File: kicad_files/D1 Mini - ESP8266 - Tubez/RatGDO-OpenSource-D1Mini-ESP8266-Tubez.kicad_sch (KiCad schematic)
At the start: 30 parts, among them J1 Screw_Terminal_01x03, J2 Conn_01x11, J3 Screw_Terminal_01x02, Q1 2N7002, Q2 AO3400A, Q3 AO3400A, Q4 AO3400A, U1 WeMos_D1_mini, U2 K7805-500R3

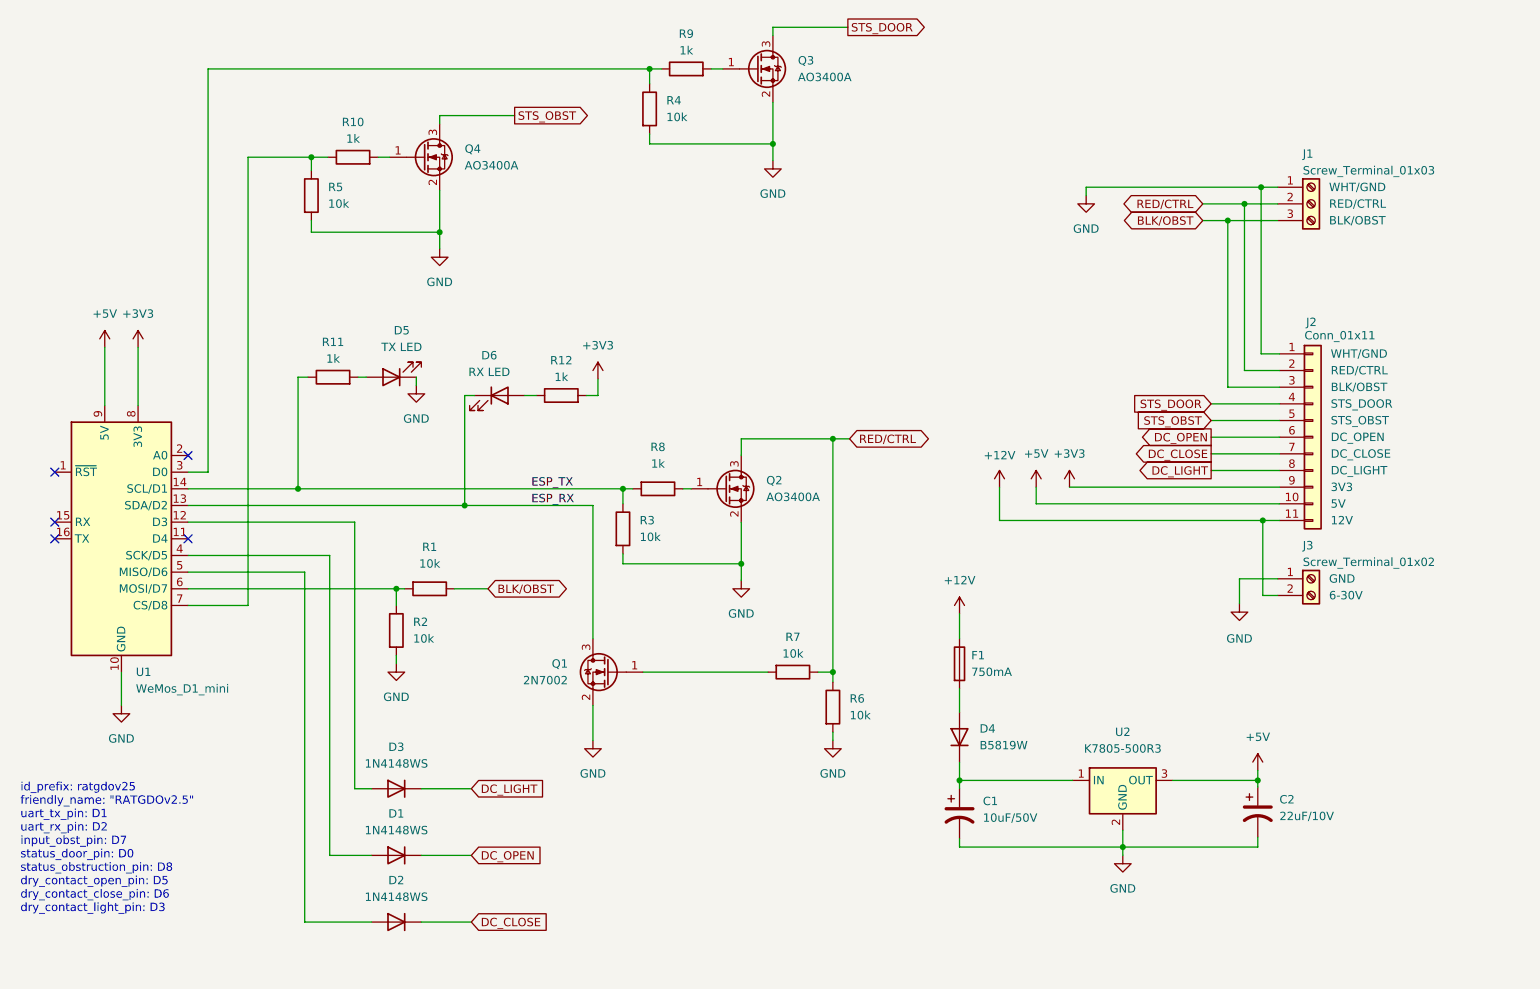
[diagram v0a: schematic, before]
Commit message: Added smt pcb jumper to switch between 5V or 3v3 supply
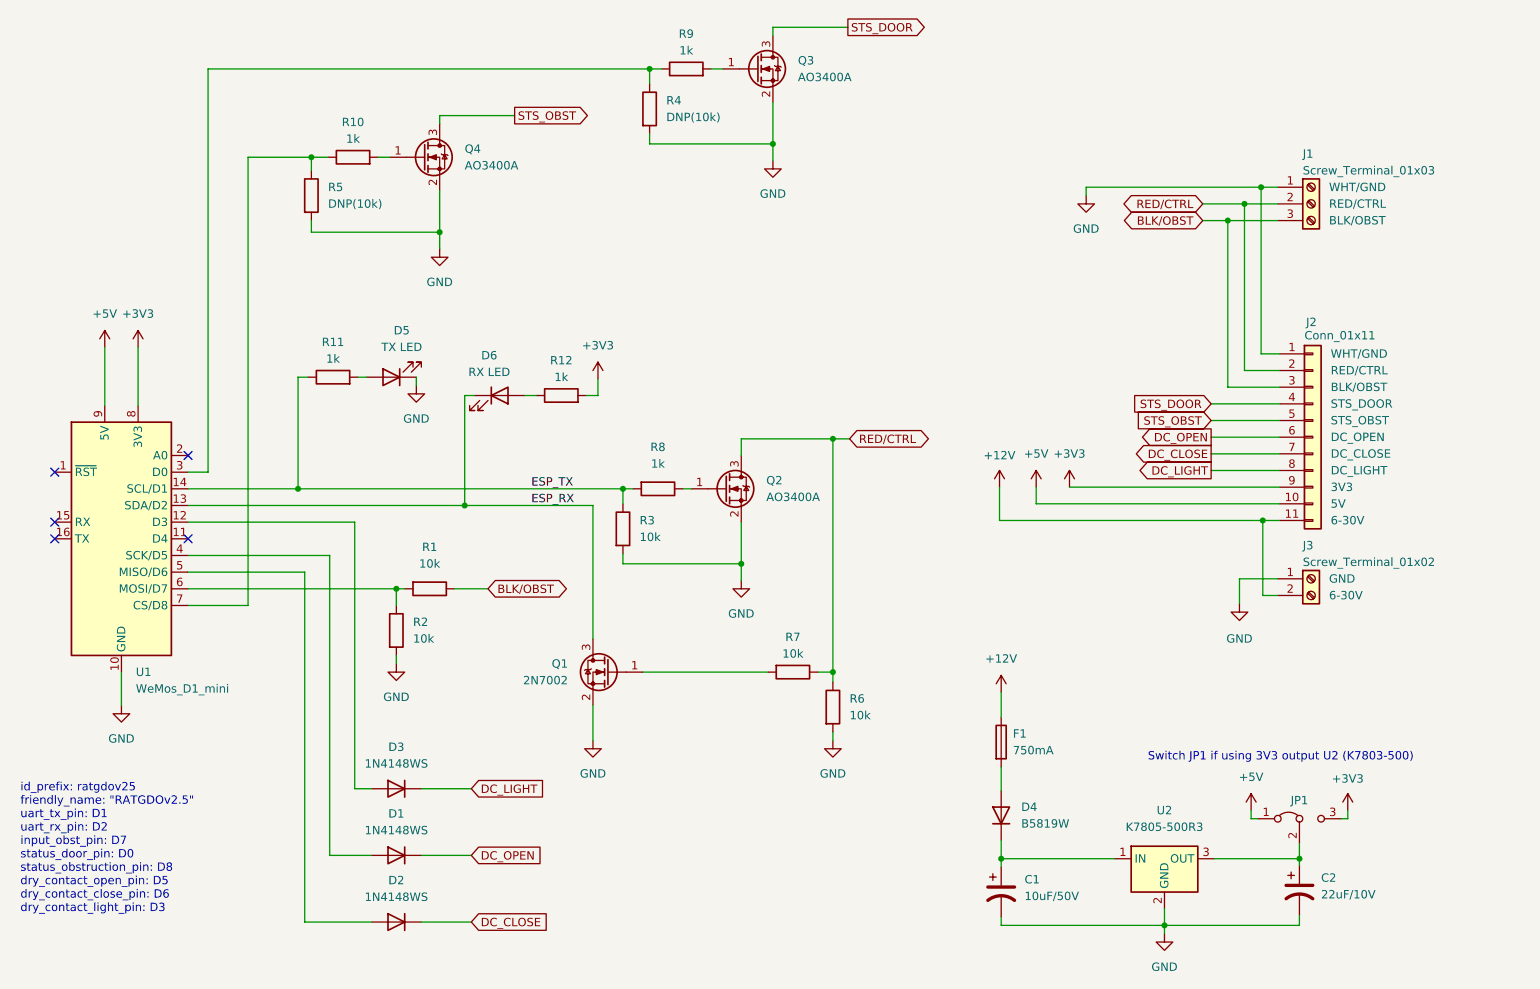
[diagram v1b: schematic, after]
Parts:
- added JP1: ~, Jumper:SolderJumper-3_P1.3mm_Bridged12_RoundedPad1.0x1.5mm, symbol Jumper:Jumper_3_Bridged12
- R4, R5: value 10k -> DNP(10k)
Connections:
- net +3V3: now also JP1.3 (B)
- net +5V: now also JP1.1 (A); no longer C2.1, U2.3 (OUT)
- new net: C2.1, JP1.2 (C), U2.3 (OUT)
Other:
- note added: "Switch JP1 if using 3V3 output U2 (K7803-500)"
- moved on the sheet: C1, C2, D4, F1, U2

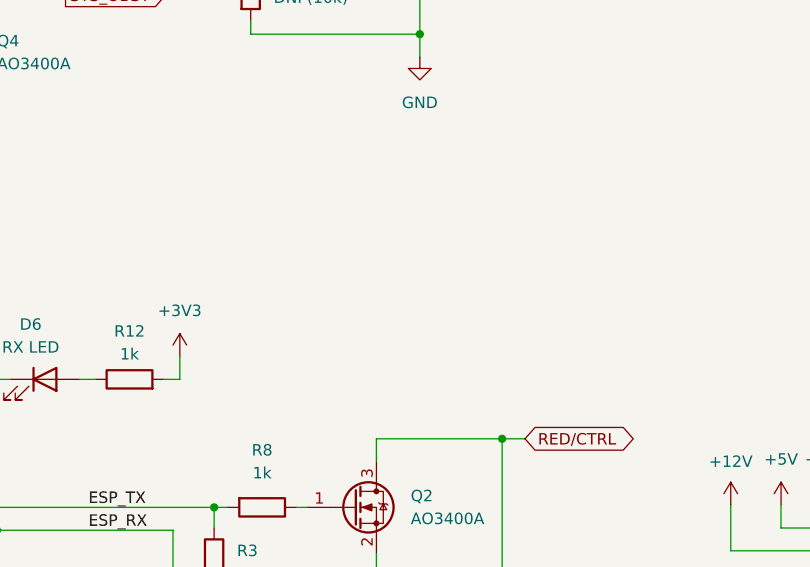
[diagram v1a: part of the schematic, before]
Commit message: schematic note and resize of min silk text height
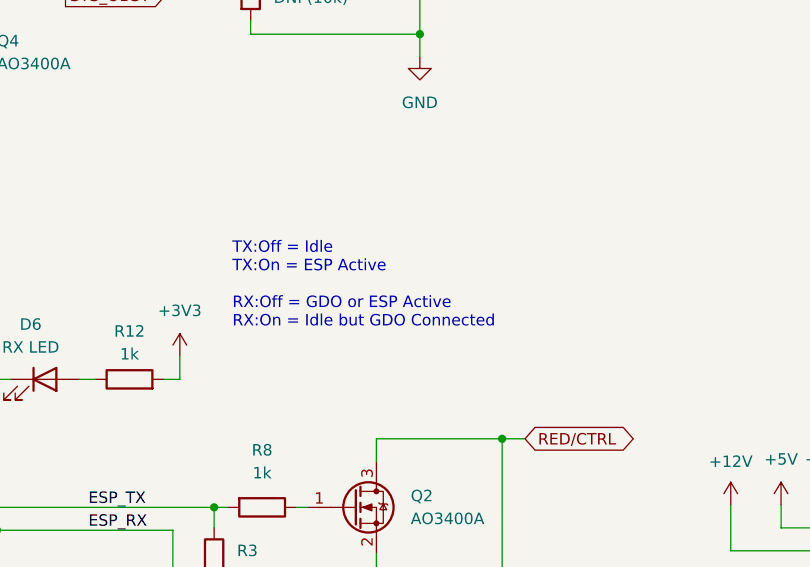
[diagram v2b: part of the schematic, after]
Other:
- note added: "TX:Off = Idle TX:On = ESP Active RX:Off = GDO or ESP Active RX:On = Idle but GDO Connected"
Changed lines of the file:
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@@
+    (effects (font (size 1.27 1.27)) (justify left bottom))
+  )
+  (text "TX:Off = Idle \nTX:On = ESP Active\n\nRX:Off = GDO or ESP Active \nRX:On = Idle but GDO Connected"
+    (at 122.936 74.168 0)
     (effects (font (size 1.27 1.27)) (justify left bottom))
   )

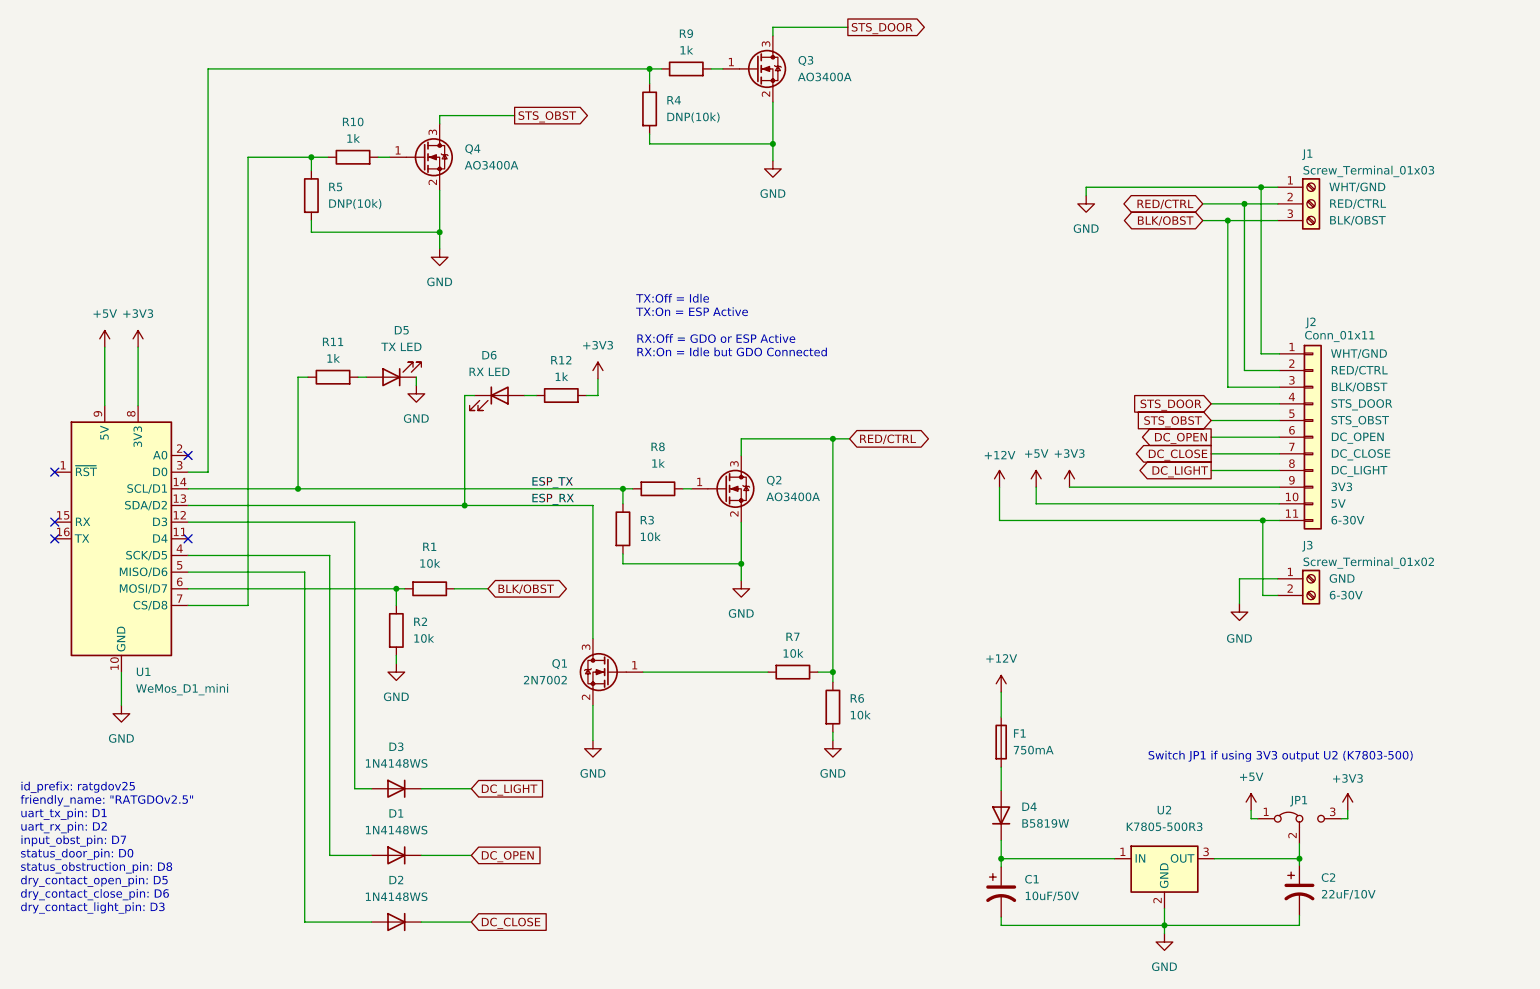
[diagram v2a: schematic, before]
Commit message: Add LED legend and move schematic onto grid
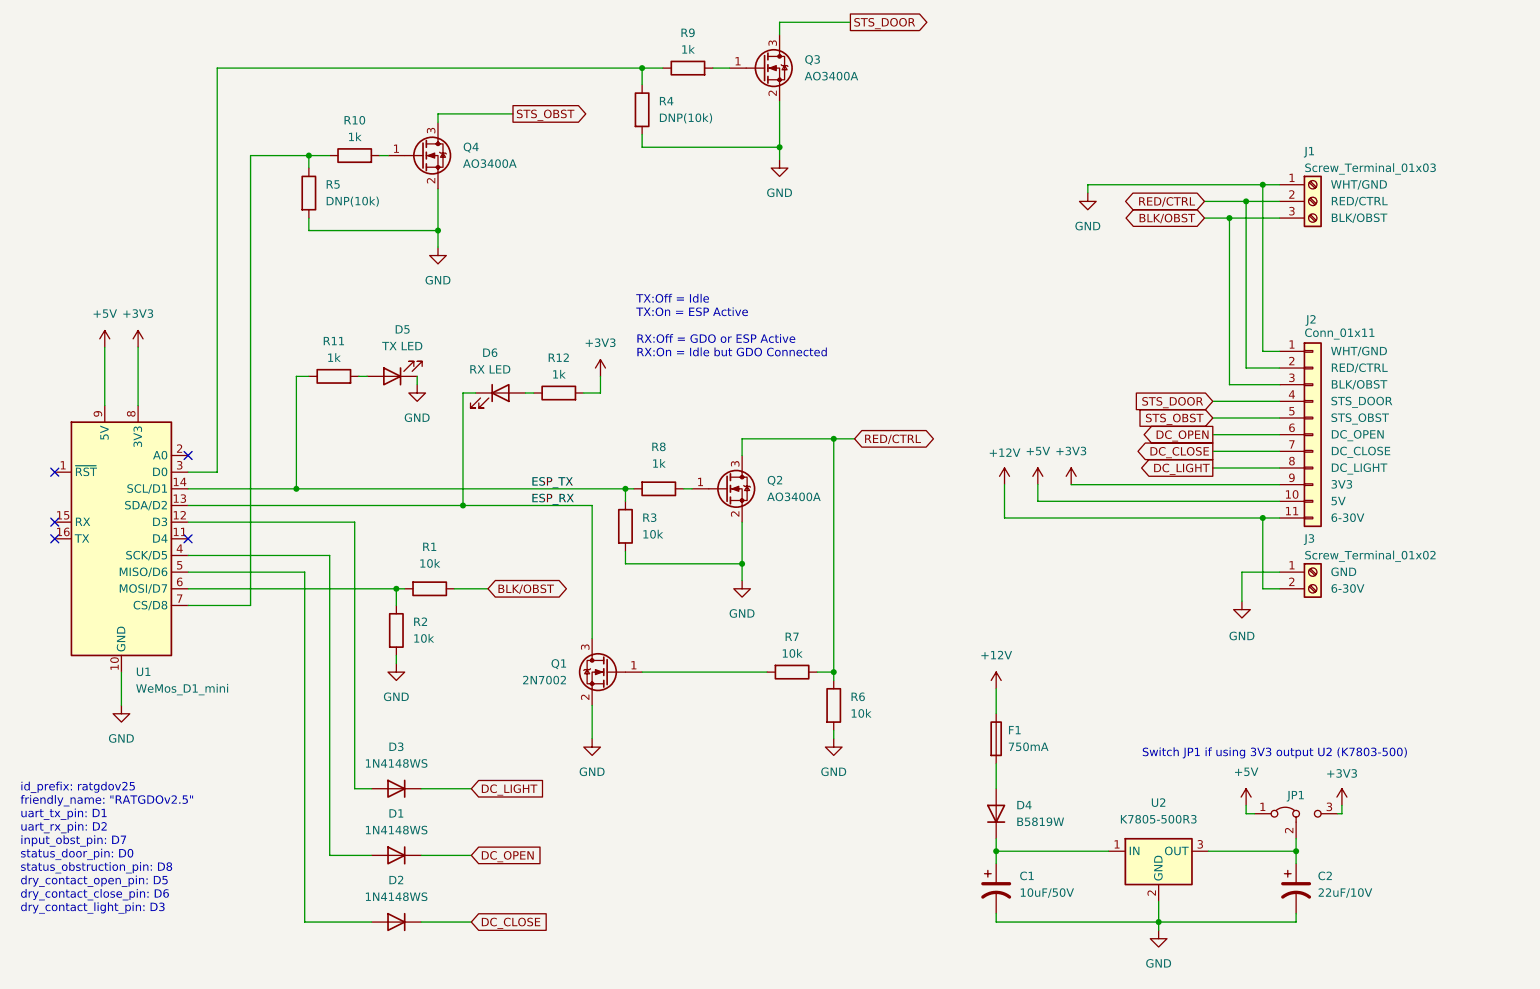
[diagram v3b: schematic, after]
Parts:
- J2: footprint Connector_PinHeader_2.54mm:PinHeader_1x11_P2.54mm_Vertical -> Custom Library:PinHeader_1x11_P2.54mm_Vertical_ExtendedPads
- JP1: footprint Jumper:SolderJumper-3_P1.3mm_Bridged12_RoundedPad1.0x1.5mm -> Custom Library:SolderJumper-3_P1.3mm_Bridged2Bar12_RoundedPad1.0x1.5mm_voltjump
- U2: footprint Converter_DCDC:Converter_DCDC_RECOM_R-78HB-0.5_THT -> Custom Library:Converter_DCDC_RECOM_R-78HB-0.5_THT_JLC_small
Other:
- moved on the sheet: C1, C2, D4, F1, J3, JP1, Q3, R12, R3, R4, R5, U2

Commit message: Designator notation swap
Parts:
- R10: renamed from R5; value DNP(10k) -> DNP
- R4: renamed from R9; value 1k -> 10k
- R5: renamed from R10; value 1k -> 10k
- R9: renamed from R4; value DNP(10k) -> DNP
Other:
- note added: "Switch JP1 if using 3V3 output U2 (K7803-500R3)"
- note removed: "Switch JP1 if using 3V3 output U2 (K7803-500)"
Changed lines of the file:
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@@
     (stroke (width 0) (type default))
   )
-  (wire (pts (xy 89.535 76.835) (xy 89.535 78.105))
+  (wire (pts (xy 90.805 76.835) (xy 89.535 76.835))
+    (stroke (width 0) (type default))
+  )
+  (wire (pts (xy 90.805 76.835) (xy 90.805 78.105))
     (stroke (width 0) (type default))
   )
@@
     (stroke (width 0) (type default))
   )
-  (text "Switch JP1 if using 3V3 output U2 (K7803-500)" (at 200.025 135.128 0)
+  (text "Switch JP1 if using 3V3 output U2 (K7803-500R3)" (at 200.025 135.128 0)
     (effects (font (size 1.27 1.27)) (justify left bottom))
   )
@@
   (symbol (lib_id "Device:R") (at 73.025 48.895 0) (unit 1)
     (in_bom yes) (on_board yes) (dnp no) (fields_autoplaced)
-    (property "Reference" "R5" (at 75.565 47.625 0)
-      (effects (font (size 1.27 1.27)) (justify left))
-    )
-    (property "Value" "DNP(10k)" (at 75.565 50.165 0)
+    (property "Reference" "R10" (at 74.93 47.625 0)
+      (effects (font (size 1.27 1.27)) (justify left))
+    )
+    (property "Value" "DNP" (at 74.93 50.165 0)
       (effects (font (size 1.27 1.27)) (justify left))
     )
@@
       (project "RatGDO-OpenSource-D1Mini-ESP8266-Tubez"
         (path "/d526daf5-1a87-4c4a-b8db-6120ccadc008"
-          (reference "R5") (unit 1)
+          (reference "R10") (unit 1)
         )
       )
@@
     )
   )
-  (symbol (lib_id "power:GND") (at 89.535 78.105 0) (unit 1)
-    (in_bom yes) (on_board yes) (dnp no) (fields_autoplaced)
-    (property "Reference" "#PWR018" (at 89.535 84.455 0)
-      (effects (font (size 1.27 1.27)) hide)
-    )
-    (property "Value" "GND" (at 89.535 83.185 0)
-      (effects (font (size 1.27 1.27)))
-    )
-    (property "Footprint" "" (at 89.535 78.105 0)
-      (effects (font (size 1.27 1.27)) hide)
-    )
-    (property "Datasheet" "" (at 89.535 78.105 0)
+  (symbol (lib_id "power:GND") (at 90.805 78.105 0) (unit 1)
+    (in_bom yes) (on_board yes) (dnp no) (fields_autoplaced)
+    (property "Reference" "#PWR018" (at 90.805 84.455 0)
+      (effects (font (size 1.27 1.27)) hide)
+    )
+    (property "Value" "GND" (at 90.805 83.185 0)
+      (effects (font (size 1.27 1.27)))
+    )
+    (property "Footprint" "" (at 90.805 78.105 0)
+      (effects (font (size 1.27 1.27)) hide)
+    )
+    (property "Datasheet" "" (at 90.805 78.105 0)
       (effects (font (size 1.27 1.27)) hide)
     )
@@
   (symbol (lib_id "Device:R") (at 123.825 36.195 0) (unit 1)
     (in_bom yes) (on_board yes) (dnp no) (fields_autoplaced)
-    (property "Reference" "R4" (at 126.365 34.925 0)
-      (effects (font (size 1.27 1.27)) (justify left))
-    )
-    (property "Value" "DNP(10k)" (at 126.365 37.465 0)
+    (property "Reference" "R9" (at 125.73 34.925 0)
+      (effects (font (size 1.27 1.27)) (justify left))
+    )
+    (property "Value" "DNP" (at 125.73 37.465 0)
       (effects (font (size 1.27 1.27)) (justify left))
     )
@@
       (project "RatGDO-OpenSource-D1Mini-ESP8266-Tubez"
         (path "/d526daf5-1a87-4c4a-b8db-6120ccadc008"
-          (reference "R4") (unit 1)
+          (reference "R9") (unit 1)
         )
       )
@@
   (symbol (lib_id "Device:R") (at 130.81 29.845 90) (unit 1)
     (in_bom yes) (on_board yes) (dnp no) (fields_autoplaced)
-    (property "Reference" "R9" (at 130.81 24.511 90)
-      (effects (font (size 1.27 1.27)))
-    )
-    (property "Value" "1k" (at 130.81 27.051 90)
+    (property "Reference" "R4" (at 130.81 24.13 90)
+      (effects (font (size 1.27 1.27)))
+    )
+    (property "Value" "10k" (at 130.81 26.67 90)
       (effects (font (size 1.27 1.27)))
     )
@@
       (project "RatGDO-OpenSource-D1Mini-ESP8266-Tubez"
         (path "/d526daf5-1a87-4c4a-b8db-6120ccadc008"
-          (reference "R9") (unit 1)
+          (reference "R4") (unit 1)
         )
       )
@@
   (symbol (lib_id "Device:R") (at 80.01 43.18 90) (unit 1)
     (in_bom yes) (on_board yes) (dnp no) (fields_autoplaced)
-    (property "Reference" "R10" (at 80.01 37.846 90)
-      (effects (font (size 1.27 1.27)))
-    )
-    (property "Value" "1k" (at 80.01 40.386 90)
+    (property "Reference" "R5" (at 80.01 36.83 90)
+      (effects (font (size 1.27 1.27)))
+    )
+    (property "Value" "10k" (at 80.01 39.37 90)
       (effects (font (size 1.27 1.27)))
     )
@@
       (project "RatGDO-OpenSource-D1Mini-ESP8266-Tubez"
         (path "/d526daf5-1a87-4c4a-b8db-6120ccadc008"
-          (reference "R10") (unit 1)
-        )
-      )
+          (reference "R5") (unit 1)
+        )
+      )
